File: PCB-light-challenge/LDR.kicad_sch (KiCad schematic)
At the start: 1 part, among them J2 Conn_01x04_Socket

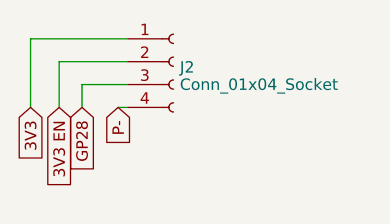
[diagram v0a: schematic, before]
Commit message: 3V3 OUT voor RGB toegevoegd en footprint van connectoren verandert naar JST
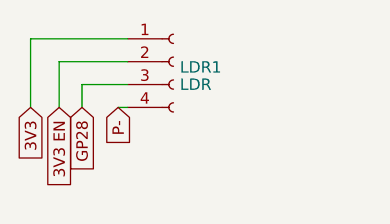
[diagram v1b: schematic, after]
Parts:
- LDR1: renamed from J2; value Conn_01x04_Socket -> LDR; footprint Connector_PinSocket_2.54mm:PinSocket_1x04_P2.54mm_Vertical -> Connector_JST:JST_EH_B4B-EH-A_1x04_P2.50mm_Vertical
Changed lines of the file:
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@@
   (symbol (lib_id "Connector:Conn_01x04_Socket") (at 133.985 85.725 0) (unit 1)
     (in_bom yes) (on_board yes) (dnp no) (fields_autoplaced)
-    (property "Reference" "J2" (at 134.6962 86.3513 0)
+    (property "Reference" "LDR1" (at 134.6962 86.3513 0)
       (effects (font (size 1.27 1.27)) (justify left))
     )
-    (property "Value" "Conn_01x04_Socket" (at 134.6962 88.2723 0)
+    (property "Value" "LDR" (at 134.6962 88.2723 0)
       (effects (font (size 1.27 1.27)) (justify left))
     )
-    (property "Footprint" "Connector_PinSocket_2.54mm:PinSocket_1x04_P2.54mm_Vertical" (at 133.985 85.725 0)
+    (property "Footprint" "Connector_JST:JST_EH_B4B-EH-A_1x04_P2.50mm_Vertical" (at 133.985 85.725 0)
       (effects (font (size 1.27 1.27)) hide)
     )
@@
       (project "PCB-light-challenge"
         (path "/35573e8f-7834-430c-81d2-239f316c7834/d6ab0385-4757-4e5e-90a4-43840d94b231"
-          (reference "J2") (unit 1)
+          (reference "LDR1") (unit 1)
         )
       )

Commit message: LDR connector, silkscreen AC,  Mounting hole main pcb aangepast
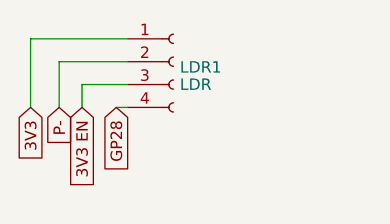
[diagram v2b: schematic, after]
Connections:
- net 3V3 EN: now also LDR1.3 (Pin_3); no longer LDR1.2 (Pin_2)
- net GP28: now also LDR1.4 (Pin_4); no longer LDR1.3 (Pin_3)
- net P-: now also LDR1.2 (Pin_2); no longer LDR1.4 (Pin_4)
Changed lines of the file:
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@@
 (kicad_sch (version 20230121) (generator eeschema)
   (paper "A4")
-  (wire (pts (xy 127.8382 90.805) (xy 128.905 90.805))
-    (stroke (width 0) (type default))
-  )
   (wire (pts (xy 121.285 85.725) (xy 121.285 90.805))
     (stroke (width 0) (type default))
@@
     (stroke (width 0) (type default))
   )
-  (global_label "GP28" (shape input) (at 123.825 90.805 270) (fields_autoplaced)
+  (wire (pts (xy 127.635 90.805) (xy 128.905 90.805))
+    (stroke (width 0) (type default))
+  )
+  (global_label "GP28" (shape input) (at 127.635 90.805 270) (fields_autoplaced)
     (effects (font (size 1.27 1.27)) (justify right))
-    (property "Intersheetrefs" "${INTERSHEET_REFS}" (at 123.825 98.6698 90)
+    (property "Intersheetrefs" "${INTERSHEET_REFS}" (at 127.635 98.6698 90)
       (effects (font (size 1.27 1.27)) (justify right) hide)
     )
@@
     )
   )
-  (global_label "3V3 EN" (shape input) (at 121.285 90.805 270) (fields_autoplaced)
+  (global_label "3V3 EN" (shape input) (at 123.825 90.805 270) (fields_autoplaced)
     (effects (font (size 1.27 1.27)) (justify right))
-    (property "Intersheetrefs" "${INTERSHEET_REFS}" (at 121.285 100.4599 90)
+    (property "Intersheetrefs" "${INTERSHEET_REFS}" (at 123.825 100.4599 90)
       (effects (font (size 1.27 1.27)) (justify right) hide)
     )
   )
-  (global_label "P-" (shape input) (at 127.8382 90.805 270) (fields_autoplaced)
+  (global_label "P-" (shape input) (at 121.285 90.805 270) (fields_autoplaced)
     (effects (font (size 1.27 1.27)) (justify right))
-    (property "Intersheetrefs" "${INTERSHEET_REFS}" (at 127.8382 96.5532 90)
+    (property "Intersheetrefs" "${INTERSHEET_REFS}" (at 121.285 96.5532 90)
       (effects (font (size 1.27 1.27)) (justify right) hide)
     )
